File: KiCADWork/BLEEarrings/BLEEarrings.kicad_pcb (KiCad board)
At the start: 2 copper layers, 44 parts, among them SW1 PB22E06071, U1 GT-USB-7010ASV, U2 2.0MM-2P WZ MS, U3 MCP73831T-2ACI/OT, U4 XB6096I2SV, U5 AP7361C-33FGE-7, U6 ESP32-C3FH4, X1 5YMA40000151SF40Q1

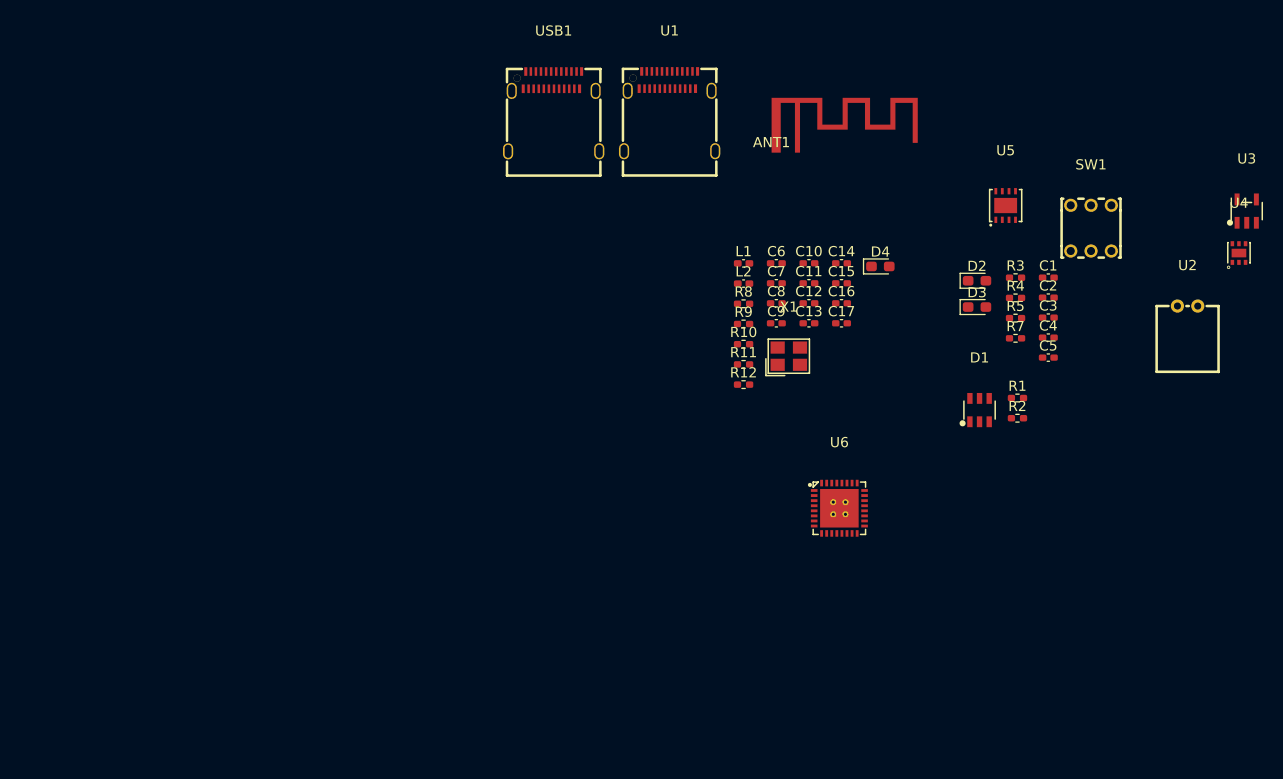
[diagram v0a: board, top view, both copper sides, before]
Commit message: Improved Antenna Layout
- Initial layout complete
- TO DO:
    - Test points
    - Curved Tracks
    - Silkscreen
    - Check antenna
    - create casing in blender
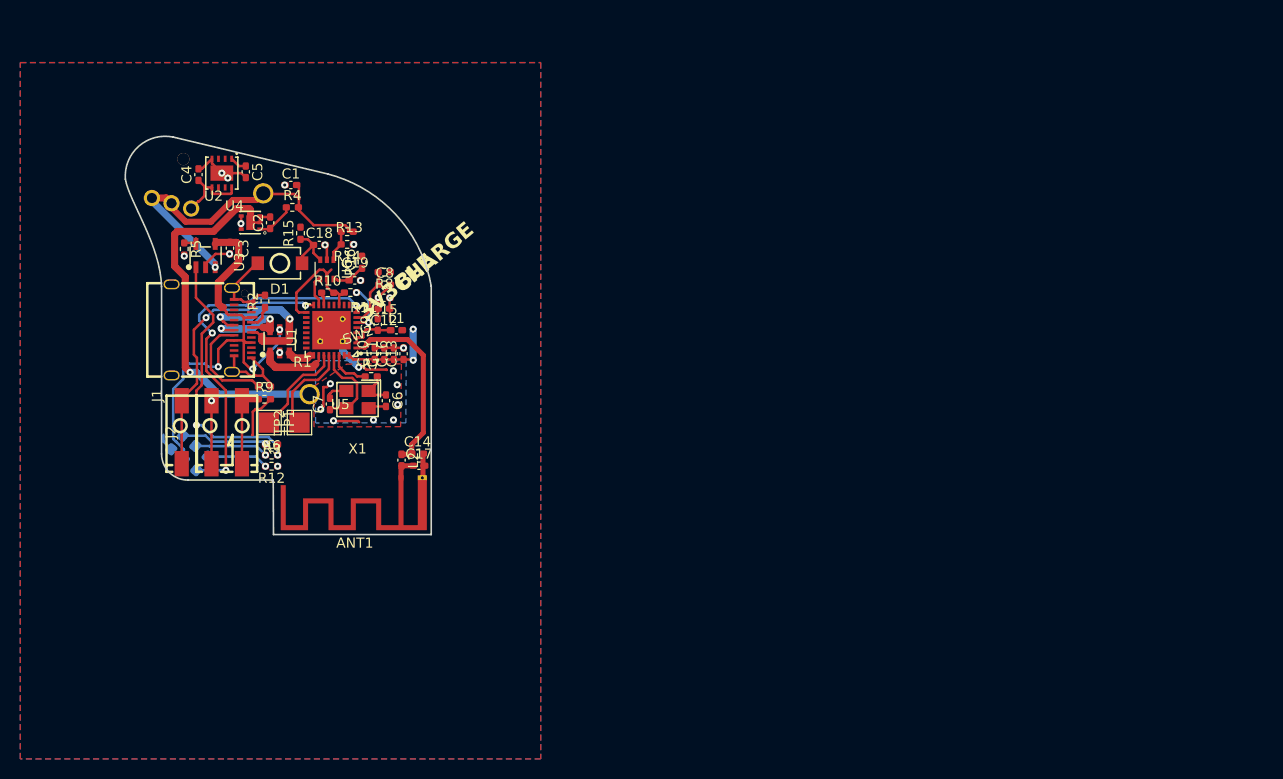
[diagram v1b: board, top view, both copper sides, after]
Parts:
- removed USB1: 12401832E402A, easyeda2kicad:USB-C-TH_12401832E402A
- added BT1: Battery, easyeda2kicad:BAT-TH_BS-24-A1AJ013, B.Cu at (150.6, 57.5)
- added C18: 100n, Capacitor_SMD:C_0402_1005Metric_Pad0.74x0.62mm_HandSolder, F.Cu at (153.8, 52.7)
- added C19: 4.7u, Capacitor_SMD:C_0402_1005Metric_Pad0.74x0.62mm_HandSolder, F.Cu at (157.3, 56.2)
- added J1: Screw_Terminal_01x01, easyeda2kicad:CONN-SMD_custom1, F.Cu at (141.8, 71.2)
- added J2: Screw_Terminal_01x02, easyeda2kicad:CONN-SMD_2059-302, F.Cu at (144.7, 71.2)
- added R13: 5k1, Resistor_SMD:R_0402_1005Metric_Pad0.72x0.64mm_HandSolder, F.Cu at (156.6, 51.4)
- added R14: 5k1, Resistor_SMD:R_0402_1005Metric_Pad0.72x0.64mm_HandSolder, F.Cu at (156.6, 52.6)
- added R15: 5k1, Resistor_SMD:R_0402_1005Metric_Pad0.72x0.64mm_HandSolder, F.Cu at (151.9, 51.5)
- added R16: 5k1, Resistor_SMD:R_0402_1005Metric_Pad0.72x0.64mm_HandSolder, F.Cu at (158.0, 54.4)
- added R6: 2k, Resistor_SMD:R_0402_1005Metric_Pad0.72x0.64mm_HandSolder, F.Cu at (149.1, 72.3)
- added SW2: RESET SWITCH, easyeda2kicad:SW-SMD_L3.9-W3.0-P4.45, F.Cu at (149.9, 54.5)
- added TP1: TestPoint, TestPoint:TestPoint_Pad_2.0x2.0mm, F.Cu at (148.8, 70.2)
- added TP2: TestPoint, TestPoint:TestPoint_Pad_2.0x2.0mm, F.Cu at (151.8, 70.2)
- ANT1: footprint CustomPads:2.4GHz, 50Ohm Antenna -> RF_Antenna:Texas_SWRA117D_2.4GHz_Right
- C7: value 4.7u -> 20pF
- C8: value 20pF -> 100n
- D2, D3, D4: moved to B.Cu
- R7: value 2k -> 22R
- R8: value 22R -> 5k1
- R9: value 5k1 -> 470
- SW1: value PB22E06071 -> TK-6580B-1; footprint easyeda2kicad:SW-TH_6P-L5.8-W5.8-P2.00-LS4.5_PB22E06371-0625 -> easyeda2kicad:SW-TH_TK-6580B-1; moved to B.Cu
- U2: value 2.0MM-2P WZ MS -> MCP73831T-2ACI/OT; footprint easyeda2kicad:CONN-TH_2P-P2.00_SHOUHAN_2.0MM-2P-WZ-MS -> easyeda2kicad:SOT-23-5_L3.0-W1.7-P0.95-LS2.8-BL
- U3: value MCP73831T-2ACI/OT -> XB6096I2SV; footprint easyeda2kicad:SOT-23-5_L3.0-W1.7-P0.95-LS2.8-BL -> easyeda2kicad:WDFN-6_L2.0-W2.0-P0.65-BL-EP
- U4: value XB6096I2SV -> AP7361C-33FGE-7; footprint easyeda2kicad:WDFN-6_L2.0-W2.0-P0.65-BL-EP -> easyeda2kicad:DFN-8_L3.0-W3.0-P0.65-BL-EP
- U5: value AP7361C-33FGE-7 -> ESP32-C3FH4; footprint easyeda2kicad:DFN-8_L3.0-W3.0-P0.65-BL-EP -> easyeda2kicad:QFN-32_L5.0-W5.0-P0.50-TL-EP3.7
- U6: value ESP32-C3FH4 -> TS5A3159ADCKR; footprint easyeda2kicad:QFN-32_L5.0-W5.0-P0.50-TL-EP3.7 -> Package_TO_SOT_SMD:SOT-363_SC-70-6
- moved U4 100.5 mm to (144.2, 45.6), turned to 180 degrees
- moved U3 98.1 mm to (147.0, 50.5), turned to 90 degrees
- moved U2 96.9 mm to (142.6, 53.8)
- moved SW1 90.6 mm to (139.2, 48.6), turned to -15 degrees
- moved C4 85.2 mm to (141.9, 45.8), turned to 90 degrees
- moved R5 82.2 mm to (140.5, 53.1), turned to -90 degrees
- moved C5 81.1 mm to (146.6, 45.5), turned to -90 degrees
- moved C3 80.9 mm to (145.0, 53.0), turned to -90 degrees
- moved D3 79.9 mm to (139.8, 72.2), turned to 50 degrees
- moved D2 79.4 mm to (141.0, 73.2), turned to -130 degrees
- moved C2 77.0 mm to (149.0, 50.5), turned to 90 degrees
- moved R3 75.3 mm to (149.1, 73.4)
- moved C1 75.2 mm to (151.0, 46.8), turned to 180 degrees
- moved R2 75.0 mm to (148.4, 58.2), turned to 90 degrees
- moved R1 74.2 mm to (148.4, 66.7)
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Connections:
- net Net-(U1-DN1) renamed /D1-
- net Net-(U1-DP1) renamed /D1+
- C1 pad 1: /Power/VBAT -> +BATT
- C14 pad 1: Net-(U6-LNA_IN) -> Net-(U5-LNA_IN)
- C17 pad 1: Net-(ANT1-P) -> Net-(ANT1-FP)
- C2 pad 1: Net-(U4-VDD) -> Net-(U3-VDD)
- C4 pad 1: Net-(U5-EN) -> Net-(U4-EN)
- C7 pad 1: Net-(U6-CHIP_EN) -> Net-(U5-XTAL_N)
- C8 pad 1: Net-(U6-XTAL_N) -> Net-(U5-CHIP_EN)
- D1 pad 1: /DSP/MCU_USB_D_P -> /D+
- D1 pad 3: /DSP/MCU_USB_D_N -> /D-
- L2 pad 1: Net-(U6-LNA_IN) -> Net-(U5-LNA_IN)
- L2 pad 2: Net-(ANT1-P) -> Net-(ANT1-FP)
- R10 pad 1: Net-(U6-GPIO2) -> Net-(U5-GPIO8)
- R11 pad 1: Net-(U6-GPIO8) -> Net-(U5-GPIO2)
- R3 pad 2: Net-(U3-STAT) -> Net-(U2-STAT)
- R4 pad 1: Net-(U4-VDD) -> Net-(U3-VDD)
- R4 pad 2: /Power/VBAT -> +BATT
- R5 pad 1: Net-(U3-PROG) -> Net-(U2-PROG)
- R7 pad 1: +3V3 -> Net-(U5-XTAL_P)
- R7 pad 2: Net-(D3-A) -> Net-(C6-Pad1)
- R8 pad 1: Net-(U6-XTAL_P) -> +3V3
- R8 pad 2: Net-(C6-Pad1) -> Net-(U5-CHIP_EN)
- R9 pad 1: +3V3 -> Net-(J2-Pin_2)
- R9 pad 2: Net-(U6-CHIP_EN) -> +3V3
- SW1 pad 1: /Power/VBAT -> +BATT
- SW1 pad 2: /Power/VBAT -> +BATT
- SW1 pad 3: Net-(U5-EN) -> Net-(U4-EN)
- U1 pad A10: (no net) -> unconnected-(U1-RX2--PadA10)
- U1 pad A11: (no net) -> unconnected-(U1-RX2+-PadA11)
- U1 pad A2: (no net) -> unconnected-(U1-TX1+-PadA2)
- U1 pad A3: (no net) -> unconnected-(U1-TX1--PadA3)
- U1 pad B10: (no net) -> unconnected-(U1-RX1--PadB10)
- U1 pad B11: (no net) -> unconnected-(U1-RX1+-PadB11)
- U1 pad B2: (no net) -> unconnected-(U1-TX2+-PadB2)
- U1 pad B3: (no net) -> unconnected-(U1-TX2--PadB3)
- U2 pad 1: /Power/VBAT -> Net-(U2-STAT)
- U2 pad 2: /Power/BATGND -> GND
- U3 pad 1: Net-(U3-STAT) -> Net-(U3-VDD)
- U3 pad 2: GND -> /Power/BATGND
- U3 pad 3: /Power/VBAT -> /Power/BATGND
- U3 pad 4: /Power/VBUS -> GND
- U3 pad 5: Net-(U3-PROG) -> GND
- U4 pad 1: Net-(U4-VDD) -> +3V3
- U4 pad 2: /Power/BATGND -> unconnected-(U4-NC-Pad2)
- U4 pad 3: /Power/BATGND -> unconnected-(U4-ADJ/NC-Pad3)
- U4 pad 5: GND -> Net-(U4-EN)
- U4 pad 6: GND -> unconnected-(U4-NC-Pad6)
- U4 pad 7: /Power/BATGND -> unconnected-(U4-NC-Pad7)
- U5 pad 1: +3V3 -> Net-(U5-LNA_IN)
- U5 pad 2: unconnected-(U5-NC-Pad2) -> Net-(C9-Pad1)
- U5 pad 3: unconnected-(U5-ADJ/NC-Pad3) -> Net-(C9-Pad1)
- U5 pad 4: GND -> unconnected-(U5-XTAL_32K_P-Pad4)
- U5 pad 5: Net-(U5-EN) -> unconnected-(U5-XTAL_32K_N-Pad5)
- U5 pad 6: unconnected-(U5-NC-Pad6) -> Net-(U5-GPIO2)
- U5 pad 7: unconnected-(U5-NC-Pad7) -> Net-(U5-CHIP_EN)
- U5 pad 8: Net-(U5-EN) -> LED_A
- U5 pad 9: GND -> unconnected-(U5-MTMS-Pad9)
- U6 pad 1: Net-(U6-LNA_IN) -> BatRef
- U6 pad 2: Net-(C9-Pad1) -> GND
- U6 pad 3: Net-(C9-Pad1) -> Net-(SW2A-C)
- U6 pad 4: unconnected-(U6-XTAL_32K_P-Pad4) -> RESET
- U6 pad 5: unconnected-(U6-XTAL_32K_N-Pad5) -> +3V3
- U6 pad 6: Net-(U6-GPIO2) -> Net-(C19-Pad1)
- X1 pad 3: Net-(U6-XTAL_N) -> Net-(U5-XTAL_N)
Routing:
- net GND: track 0.00 -> 63.4 mm, vias 0 -> 23
- net /Power/VBUS: track 0.00 -> 43.8 mm, vias 0 -> 3
- net /Power/BATGND: track 0.00 -> 39.3 mm, vias 0 -> 1
- net LED_A: track 0.00 -> 37.0 mm, vias 0 -> 3
- net +BATT: track 0.00 -> 36.1 mm, vias 0 -> 1
- net +3V3: track 0.00 -> 31.2 mm, vias 0 -> 3
- net NEO_LED: track 0.00 -> 29.0 mm, vias 0 -> 2
- net Net-(U2-STAT): track 0.00 -> 26.7 mm, vias 0 -> 2
- net Net-(U5-LNA_IN): track 0.00 -> 19.1 mm
- net /D1-: track 0.00 -> 15.7 mm, vias 0 -> 2
- net Net-(U1-CC2): track 0.00 -> 10.5 mm
- net Net-(U5-U0RXD): track 0.00 -> 9.59 mm
- net /D1+: track 0.00 -> 9.41 mm, vias 0 -> 2
- net Net-(U5-XTAL_N): track 0.00 -> 8.68 mm
- net Net-(D3-A): track 0.00 -> 8.54 mm, vias 0 -> 1
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- added copper zone on F.Cu, net +3V3
- added copper zone on B.Cu, net GND
- added copper zone on F.Cu, net GND
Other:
- board outline added: 30.1 x 39.2 mm
- board text added: "3V3"
- board text added: "BLE"
- board text added: "CHARGE"
